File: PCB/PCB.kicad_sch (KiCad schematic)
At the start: 52 parts, among them SW1 SW_SPDT, U1 STM32L010F4Px, U4 OPA344NA

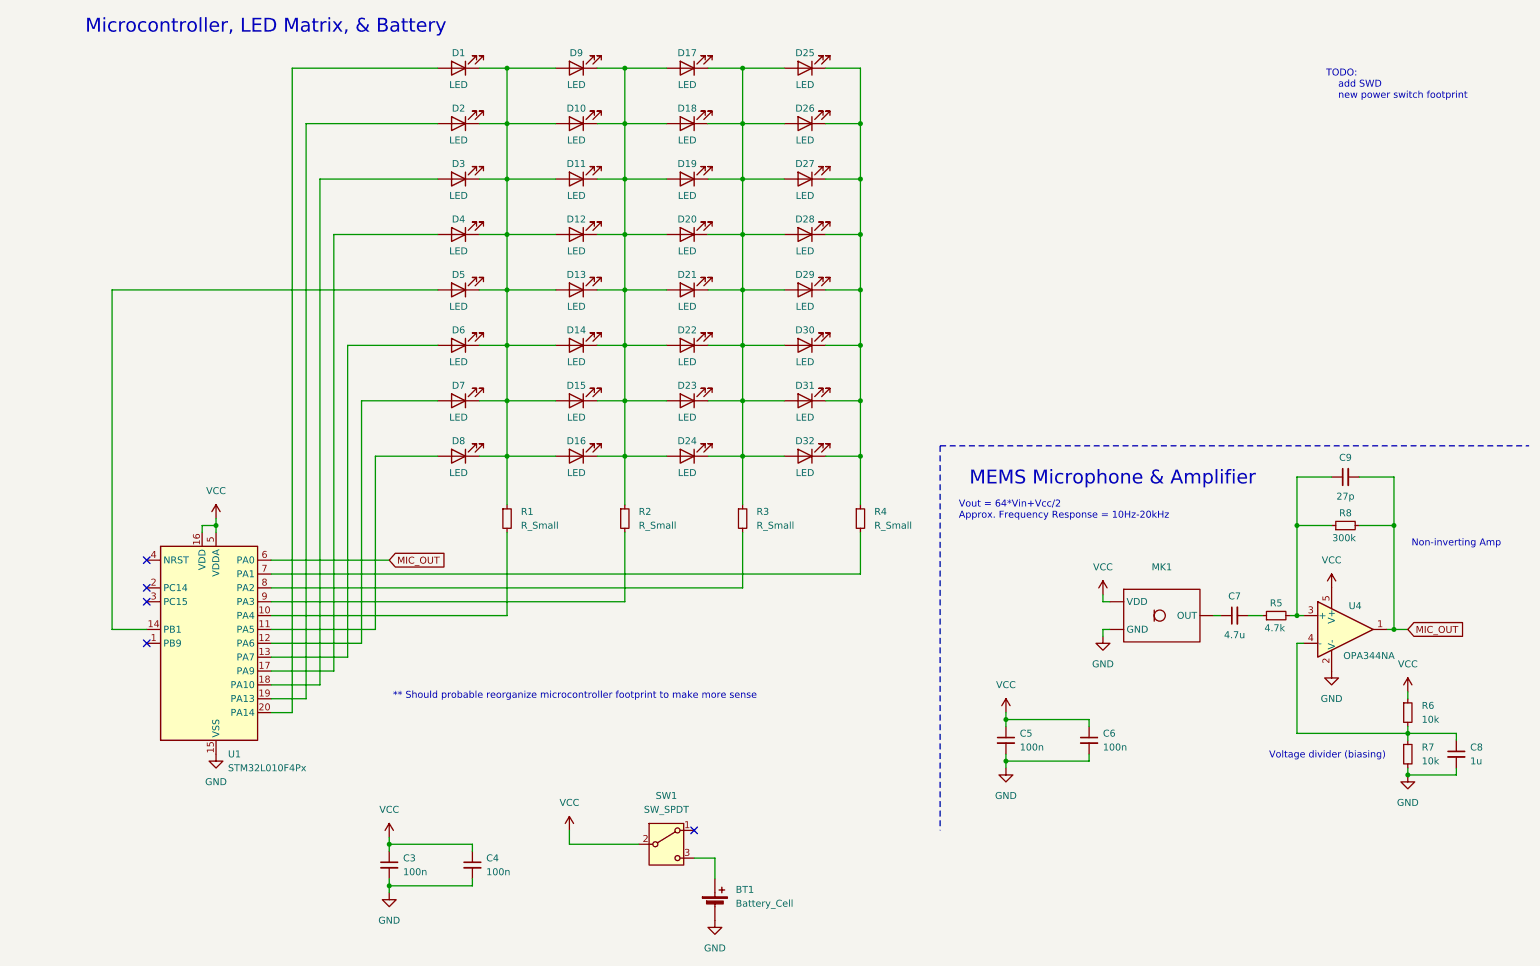
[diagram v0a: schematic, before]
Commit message: MEMS microphone, SWD, and PCB trace USB power
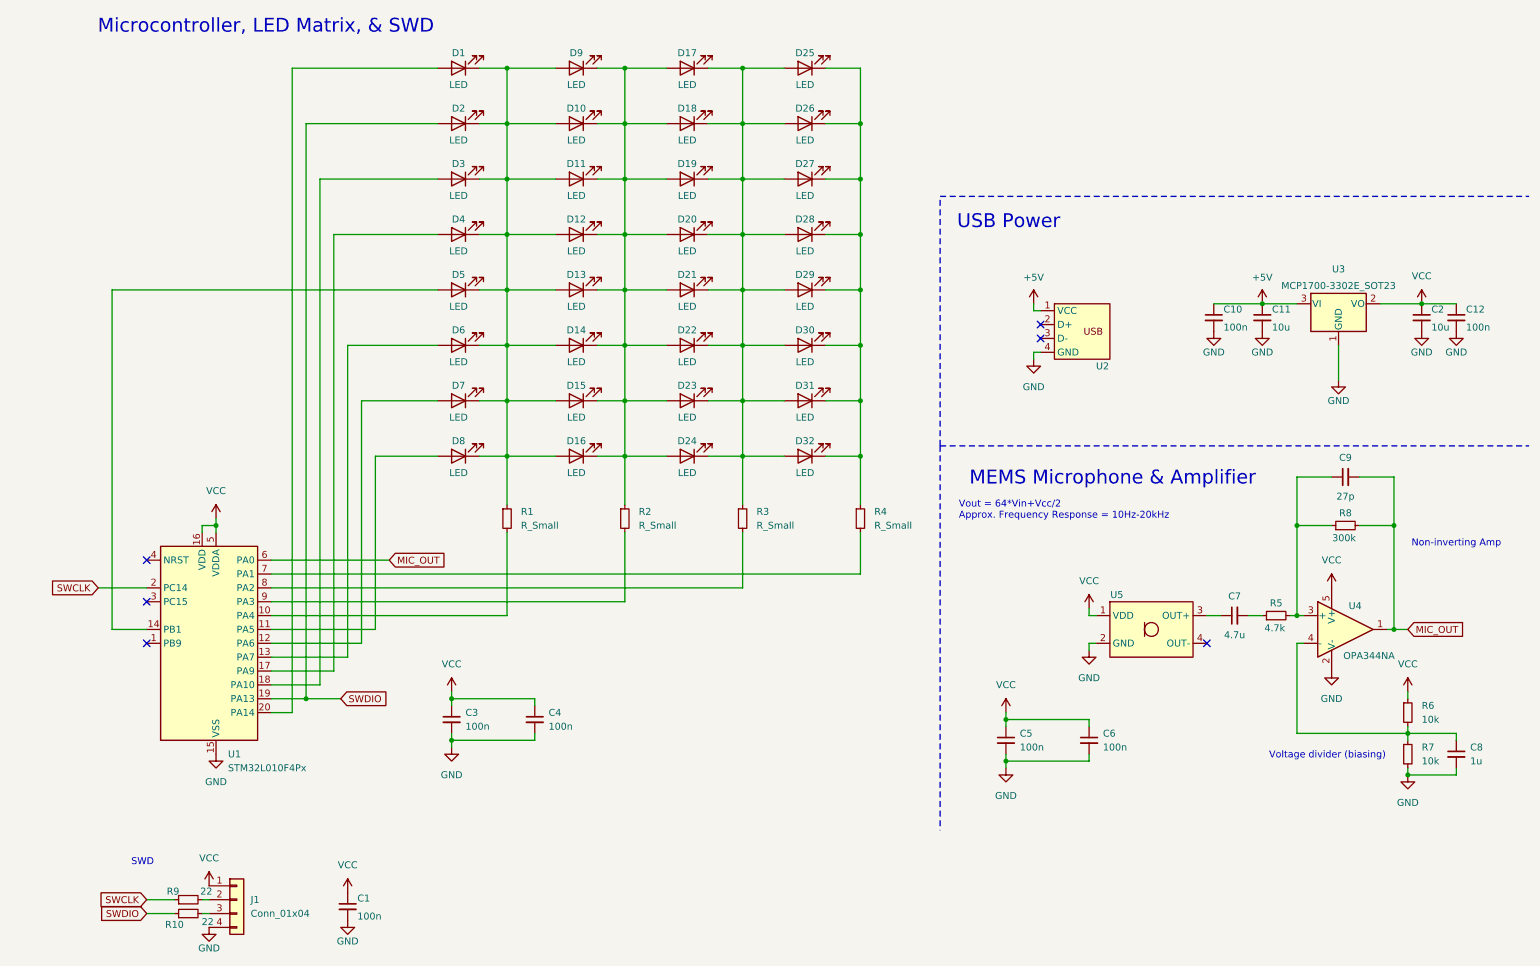
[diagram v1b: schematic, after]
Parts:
- removed BT1: Battery_Cell, 1_Custom_Parts:BAT-HLD-012-SMT_TEC, symbol Device:Battery_Cell
- removed MK1: ~, 1_Custom_Parts:ICS-40180, symbol 1_Custom_Parts:ICS-40180
- removed SW1: SW_SPDT, 1_Custom_Parts:SW_450405020524, symbol Switch:SW_SPDT
- added C1, C10, C12: 100n, Capacitor_SMD:C_0805_2012Metric, symbol Device:C_Small
- added C11, C2: 10u, Capacitor_SMD:C_0805_2012Metric, symbol Device:C_Small
- added J1: Conn_01x04, Connector_PinHeader_2.54mm:PinHeader_1x04_P2.54mm_Vertical, symbol Connector_Generic:Conn_01x04
- added R10, R9: 22, Resistor_SMD:R_0805_2012Metric, symbol Device:R_Small
- added U2: ~, 1_Custom_Parts:PCB_USB, symbol 1_Custom_Parts:PCB_USB
- added U3: MCP1700-3302E_SOT23, Package_TO_SOT_SMD:SOT-23, symbol Regulator_Linear:MCP1700-3302E_SOT23
- added U5: ~, 1_Custom_Parts:SPH8878LR5H-1, symbol 1_Custom_Parts:SPH8878LR5H-1
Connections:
- net GND: now also C1.2, C10.2, C11.2, C12.2, C2.2, J1.4 (Pin_4), U2.4 (GND), U3.1 (GND), U5.2 (GND)
- net VCC: now also C1.1, C12.1, C2.1, J1.1 (Pin_1), U3.2 (VO), U5.1 (VDD)
- net SWDIO: now reaches D2.2 (A), U1.19 (PA13)
- net SWDIO: now also R10.1
- net at C7.1: now also U5.3 (OUT+)
- net SWCLK: now reaches U1.2 (PC14)
- net SWCLK: now also R9.1
- new net: J1.2 (Pin_2), R9.2
- new net: J1.3 (Pin_3), R10.2
- new net +5V: C10.1, C11.1, U2.1 (VCC), U3.3 (VI)
- no-connect marks 5 -> 6
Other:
- note added: "Microcontroller, LED Matrix, & SWD"
- note added: "SWD"
- note added: "USB Power"
- note removed: "** Should probable reorganize microcontroller footprint to make more sense"
- note removed: "Microcontroller, LED Matrix, & Battery"
- note removed: "TODO: add SWD new power switch footprint"
- moved on the sheet: C3, C4
